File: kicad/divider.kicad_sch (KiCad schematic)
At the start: 10 parts, among them J39 SPI, Q6 2N3904, Q8 2N3904, U11 ATtiny24A-P, U14 74LS241

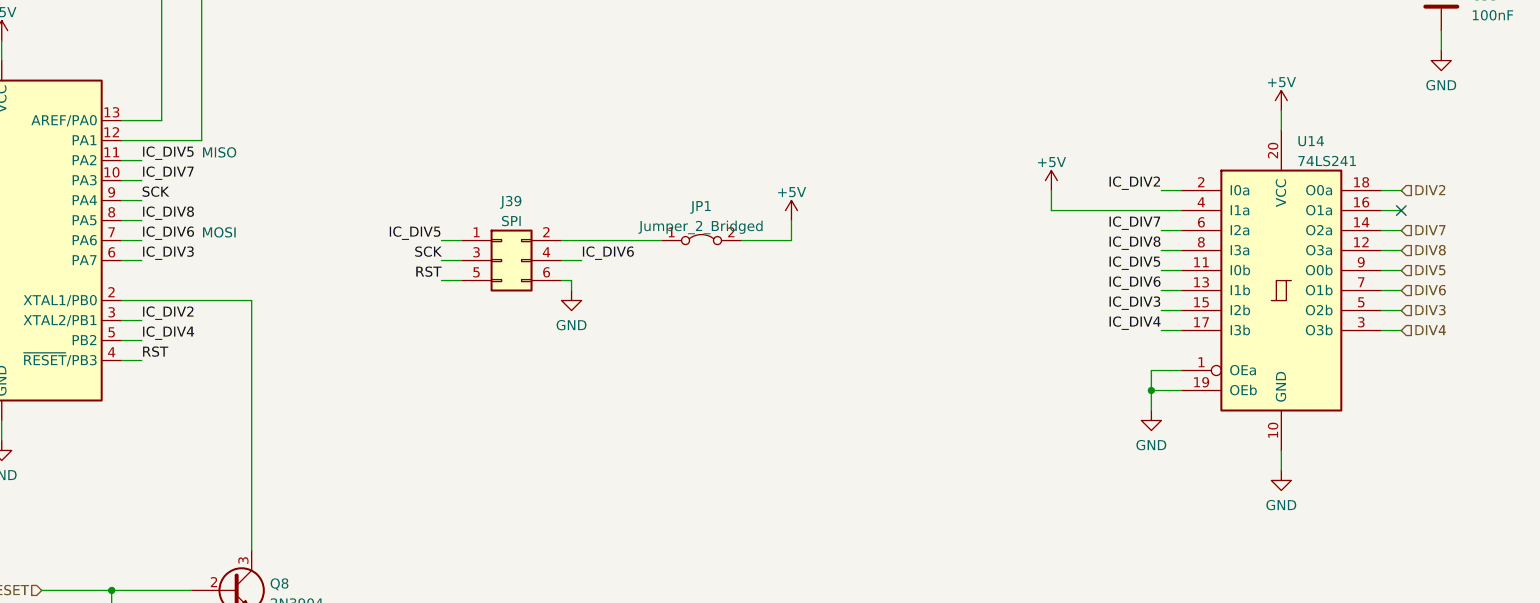
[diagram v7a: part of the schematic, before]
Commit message: Fixing issues in the divider circuitry
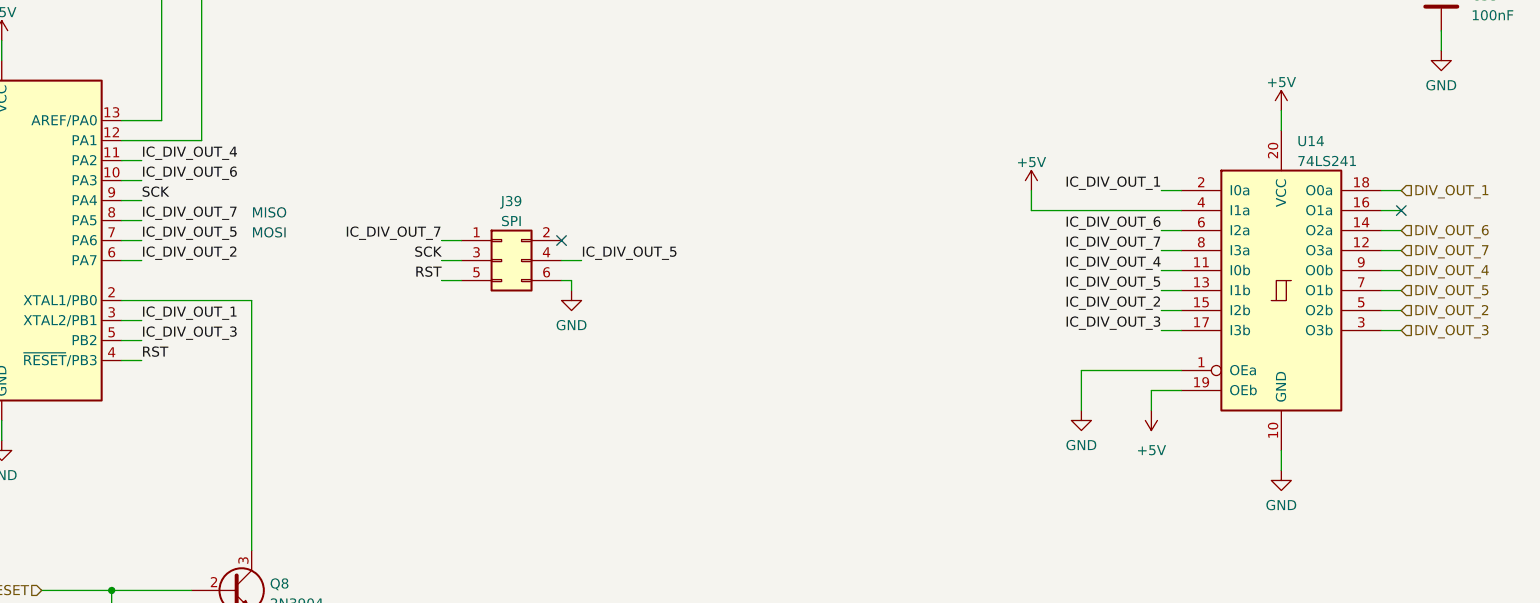
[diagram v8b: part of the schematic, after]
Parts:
- removed JP1: Jumper_2_Bridged, Connector_PinHeader_2.54mm:PinHeader_1x02_P2.54mm_Vertical, symbol Jumper:Jumper_2_Bridged
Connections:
- net +5V: now also U14.19 (OEb)
- net GND: no longer U14.19 (OEb)
- net DIV2 renamed DIV_OUT_1
- net DIV3 renamed DIV_OUT_2
- net DIV4 renamed DIV_OUT_3
- net DIV5 renamed DIV_OUT_4
- net DIV6 renamed DIV_OUT_5
- net DIV7 renamed DIV_OUT_6
- net DIV8 renamed DIV_OUT_7
- net IC_DIV2 renamed IC_DIV_OUT_1
- net IC_DIV3 renamed IC_DIV_OUT_2
- net IC_DIV4 renamed IC_DIV_OUT_3
- net IC_DIV5 renamed IC_DIV_OUT_4
- net IC_DIV_OUT_4: no longer J39.1 (Pin_1)
- net IC_DIV6 renamed IC_DIV_OUT_5
- net IC_DIV7 renamed IC_DIV_OUT_6
- net IC_DIV8 renamed IC_DIV_OUT_7
- net IC_DIV_OUT_7: now also J39.1 (Pin_1)
- no-connect marks 1 -> 2
